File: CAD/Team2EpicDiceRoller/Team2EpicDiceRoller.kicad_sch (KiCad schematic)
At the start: 48 parts, among them J1 Conn_02x03_Odd_Even, J2 Conn_01x16, J3 Conn_01x02_9VBatt, Q1 BS170, Q2 2N2222, SW1 SW_SPDT, SW2 Tilt_Switch, SW3 RotaryEncoder_Switch, SW4 SW_DPST, SW5 SW_LeftMenu, SW6 SW_MidMenu, SW7 SW_Reset, SW8 SW_RightMenu, U1 74HC14, U2 ATmega328P-P, Y1 Crystal_16MHz

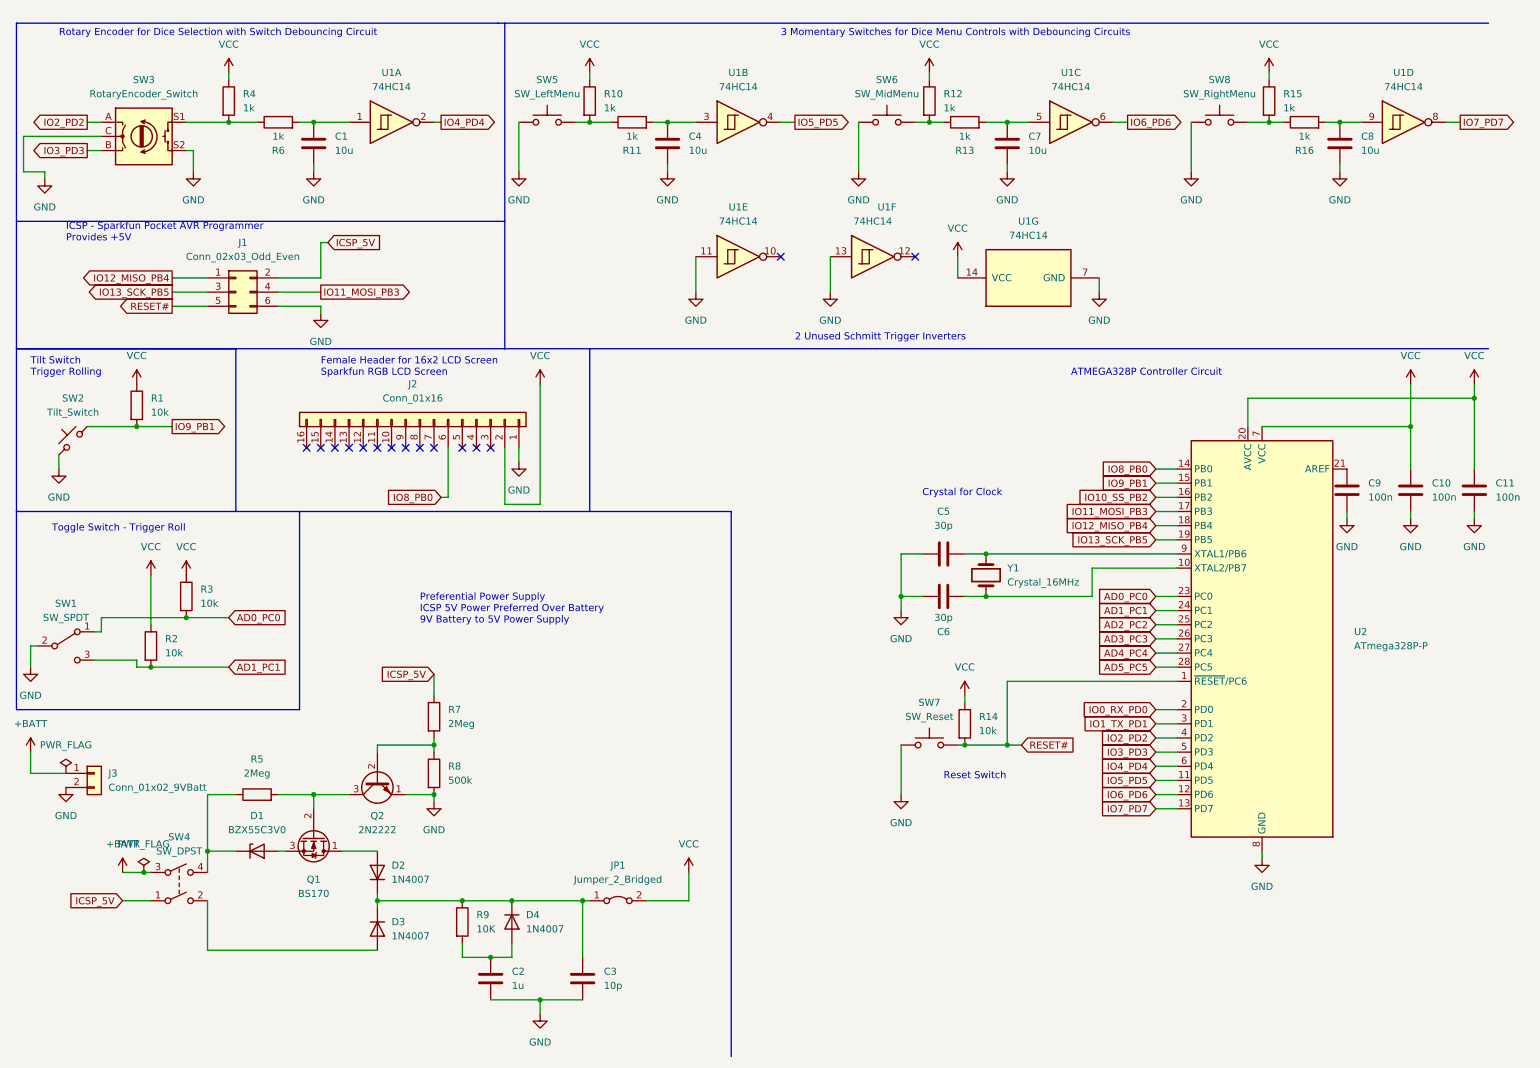
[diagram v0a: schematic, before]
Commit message: Added power supply circuit, barrel jack, logic level shifter
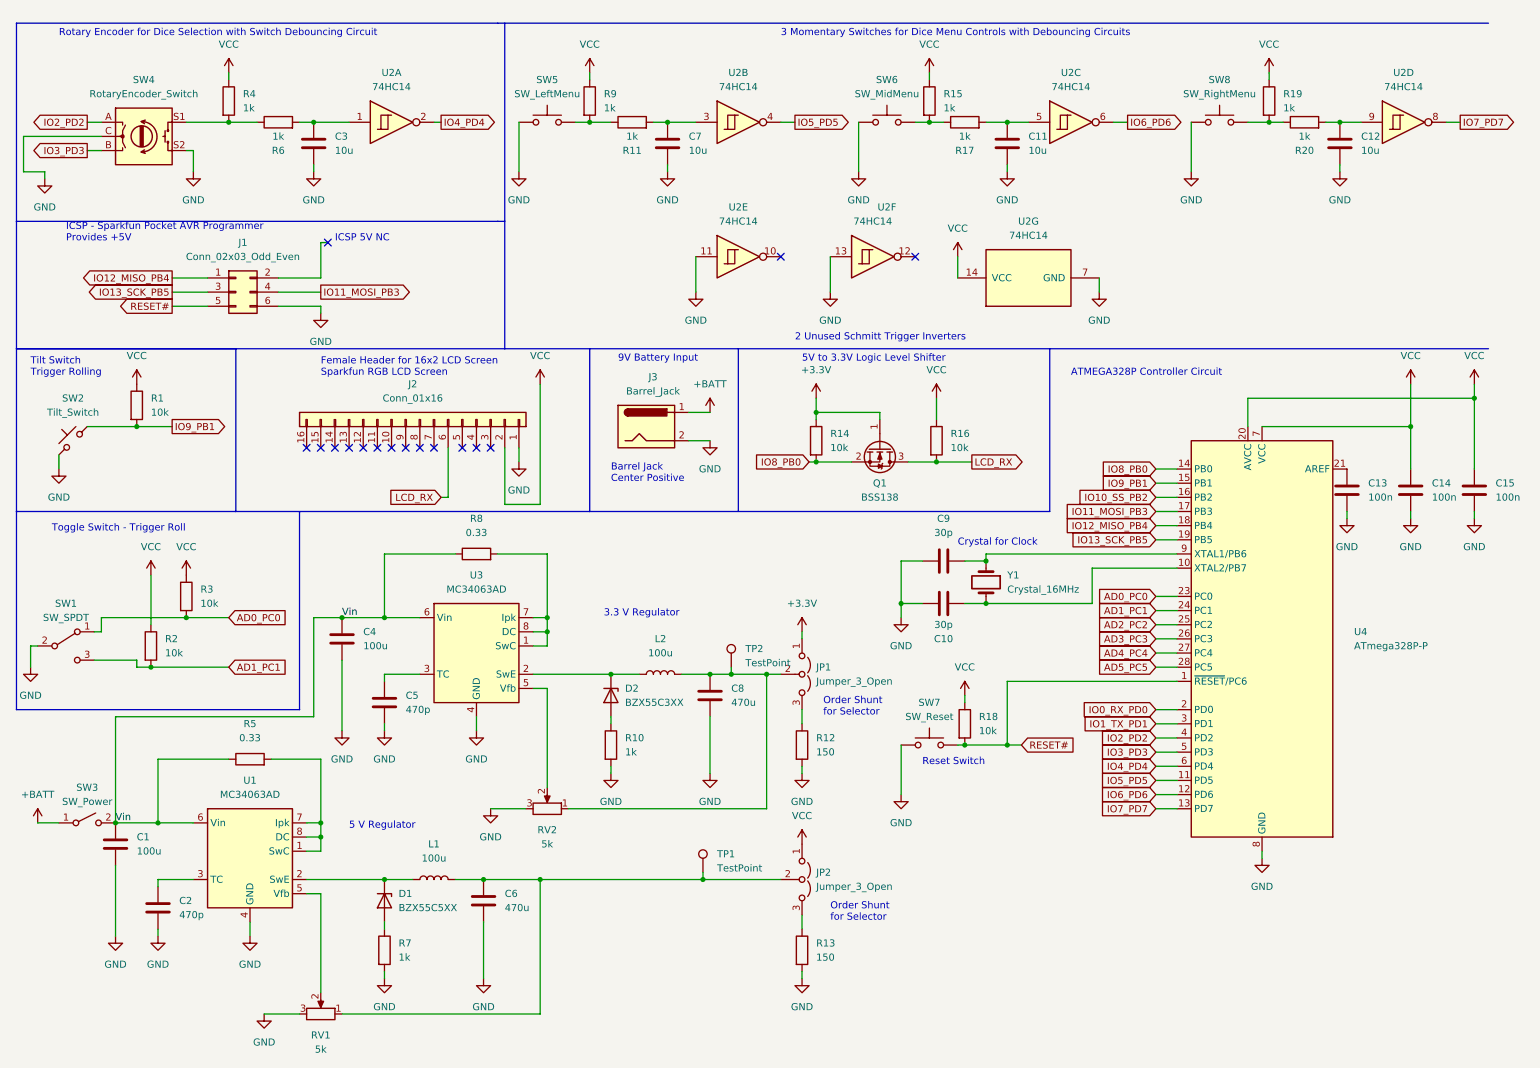
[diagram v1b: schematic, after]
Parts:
- removed D2, D3, D4: 1N4007, Diode_THT:D_DO-41_SOD81_P10.16mm_Horizontal, symbol Diode:1N4007
- removed J3: Conn_01x02_9VBatt, Connector_PinHeader_2.54mm:PinHeader_1x02_P2.54mm_Vertical, symbol Connector_Generic:Conn_01x02
- removed JP1: Jumper_2_Bridged, TestPoint:TestPoint_Bridge_Pitch2.54mm_Drill1.0mm, symbol Jumper:Jumper_2_Bridged
- removed Q1: BS170, Package_TO_SOT_THT:TO-92_Inline, symbol Transistor_FET:BS170
- removed Q2: 2N2222, Package_TO_SOT_THT:TO-92_Inline, symbol Transistor_BJT:PN2222A
- removed R5: 2Meg, Resistor_SMD:R_1206_3216Metric_Pad1.30x1.75mm_HandSolder, symbol Device:R
- removed SW4: SW_DPST, symbol Switch:SW_DPST
- added C4: 100u, Capacitor_SMD:C_1206_3216Metric_Pad1.33x1.80mm_HandSolder, symbol Device:C
- added C5: 470p, Capacitor_SMD:C_1206_3216Metric_Pad1.33x1.80mm_HandSolder, symbol Device:C
- added C6, C8: 470u, Capacitor_SMD:C_1206_3216Metric_Pad1.33x1.80mm_HandSolder, symbol Device:C
- added D2: BZX55C3XX, Diode_THT:D_DO-35_SOD27_P7.62mm_Horizontal, symbol Device:D_Zener
- added J3: Barrel_Jack, symbol Connector:Barrel_Jack
- added JP1, JP2: Jumper_3_Open, symbol Jumper:Jumper_3_Open
- added L1, L2: 100u, symbol Device:L
- added Q1: BSS138, Package_TO_SOT_SMD:SOT-23, symbol Transistor_FET:BSS138
- added R10: 1k, Resistor_SMD:R_1206_3216Metric_Pad1.30x1.75mm_HandSolder, symbol Device:R
- added R12: 150, Resistor_SMD:R_1206_3216Metric_Pad1.30x1.75mm_HandSolder, symbol Device:R
- added R14, R16: 10k, symbol Device:R
- added R8: 0.33, Resistor_SMD:R_1206_3216Metric_Pad1.30x1.75mm_HandSolder, symbol Device:R
- added RV1, RV2: 5k, symbol Device:R_Potentiometer
- added SW3: SW_Power, symbol Switch:SW_SPST
- added TP1, TP2: TestPoint, symbol Connector:TestPoint
- added U1, U3: MC34063AD, Package_SO:SOIC-8_3.9x4.9mm_P1.27mm, symbol Regulator_Switching:MC34063AD
- C1: renamed from C2; value 1u -> 100u
- C2: renamed from C3; value 10p -> 470p
- D1: value BZX55C3V0 -> BZX55C5XX
- R13: renamed from R9; value 10K -> 150
- R5: renamed from R8; value 500k -> 0.33
- R7: value 2Meg -> 1k
- renumbered C6 to C10, C7 to C11, C8 to C12, C9 to C13, C10 to C14, C11 to C15, C1 to C3, C4 to C7, C5 to C9, R12 to R15, R13 to R17, R14 to R18, R15 to R19, R16 to R20, R10 to R9, SW3 to SW4, U1 to U2, U2 to U4
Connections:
- net +BATT: now also J3.1, SW3.1 (A)
- net GND: now also R13.2, R7.2, C4.2, C5.2, C6.2, C8.2, J3.2, R10.2, R12.2, RV1.3, RV2.3, U1.4 (GND), U3.4 (GND); no longer R5.2
- net IO8_PB0: now also Q1.2 (S), R14.2; no longer J2.6 (Pin_6)
- net VCC: now also JP2.1 (A), R16.1
- net at D1.2 (A): now also R7.1
- net Vin: now reaches C1.1
- net Vin: now also R5.1, C4.1, R8.1, SW3.2 (B), U1.6 (Vin), U3.6 (Vin); no longer R13.2
- net at C2.1: now also U1.3 (TC); no longer R13.1
- net at D1.1 (K): now also L1.1, U1.2 (SwE)
- net ICSP_5V: no longer names the net of J1.2 (Pin_2)
- net ICSP_5V: no longer R7.1
- new net: C6.1, JP2.2 (C), L1.2, RV1.1, TP1.1
- new net: JP2.3 (B), R13.1
- new net: R8.2, U3.1 (SwC), U3.7 (Ipk), U3.8 (DC)
- new net: D2.1 (K), L2.1, U3.2 (SwE)
- new net: C5.1, U3.3 (TC)
- new net: RV2.2, U3.5 (Vfb)
- new net: R5.2, U1.1 (SwC), U1.7 (Ipk), U1.8 (DC)
- new net: RV1.2, U1.5 (Vfb)
- new net: JP1.3 (B), R12.1
- new net: C8.1, JP1.2 (C), L2.2, RV2.1, TP2.1
- new net: D2.2 (A), R10.1
- new net +3V3: JP1.1 (A), Q1.1 (G), R14.1
- new net LCD_RX: J2.6 (Pin_6), Q1.3 (D), R16.2
- no-connect marks 15 -> 16
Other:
- note added: "3.3 V Regulator"
- note added: "5 V Regulator"
- note added: "5V to 3.3V Logic Level Shifter"
- note added: "9V Battery Input"
- note added: "Barrel Jack Center Positive"
- note added: "ICSP 5V NC"
- note added: "Order Shunt for Selector"
- note removed: "Preferential Power Supply ICSP 5V Power Preferred Over Battery 9V Battery to 5V Power Supply"
- title: Team 2 - Dice Roller Initial Schematic -> Team 2 - Dice Roller Schematic
- moved on the sheet: C1, C10, C2, C9, D1, R13, R5, R7, Y1

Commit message: Updated schematic
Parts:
- J3: footprint (none) -> Library:BarrelJack_CUI_PJ-037A_Horizontal
- JP1, JP2: footprint (none) -> Connector_PinHeader_2.54mm:PinHeader_1x03_P2.54mm_Vertical
- Q1: footprint Package_TO_SOT_SMD:SOT-23 -> Package_TO_SOT_SMD:SOT-323_SC-70_Handsoldering
- R14, R16: footprint (none) -> Resistor_SMD:R_1206_3216Metric_Pad1.30x1.75mm_HandSolder
- RV1, RV2: footprint (none) -> Library:TRIM_TC33X-2-502E
- SW1: value SW_SPDT -> SW_Toggle_SPDT; footprint (none) -> Library:GoldSun_MTS103_Mini_Toggle_Switch
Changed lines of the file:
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@@
       (effects (font (size 1.27 1.27)) (justify left))
     )
-    (property "Footprint" "" (id 2) (at 155.702 87.63 90)
+    (property "Footprint" "Resistor_SMD:R_1206_3216Metric_Pad1.30x1.75mm_HandSolder" (id 2) (at 155.702 87.63 90)
       (effects (font (size 1.27 1.27)) hide)
     )
@@
       (effects (font (size 1.27 1.27)) (justify left))
     )
-    (property "Footprint" "" (id 2) (at 177.292 87.63 90)
+    (property "Footprint" "Resistor_SMD:R_1206_3216Metric_Pad1.30x1.75mm_HandSolder" (id 2) (at 177.292 87.63 90)
       (effects (font (size 1.27 1.27)) hide)
     )
@@
     (property "Reference" "RV1" (id 0) (at 68.58 194.31 90))
     (property "Value" "5k" (id 1) (at 68.58 196.85 90))
-    (property "Footprint" "" (id 2) (at 68.58 190.5 0)
+    (property "Footprint" "Library:TRIM_TC33X-2-502E" (id 2) (at 68.58 190.5 0)
       (effects (font (size 1.27 1.27)) hide)
     )
@@
     (property "Reference" "RV2" (id 0) (at 109.22 157.48 90))
     (property "Value" "5k" (id 1) (at 109.22 160.02 90))
-    (property "Footprint" "" (id 2) (at 109.22 153.67 0)
+    (property "Footprint" "Library:TRIM_TC33X-2-502E" (id 2) (at 109.22 153.67 0)
       (effects (font (size 1.27 1.27)) hide)
     )
@@
     (in_bom yes) (on_board yes) (fields_autoplaced)
     (property "Reference" "SW1" (id 0) (at 22.86 116.84 0))
-    (property "Value" "SW_SPDT" (id 1) (at 22.86 119.38 0))
-    (property "Footprint" "" (id 2) (at 22.86 124.46 0)
+    (property "Value" "SW_Toggle_SPDT" (id 1) (at 22.86 119.38 0))
+    (property "Footprint" "Library:GoldSun_MTS103_Mini_Toggle_Switch" (id 2) (at 22.86 124.46 0)
       (effects (font (size 1.27 1.27)) hide)
     )
@@
       (effects (font (size 1.27 1.27)) (justify left))
     )
-    (property "Footprint" "" (id 2) (at 154.94 129.54 0)
+    (property "Footprint" "Connector_PinHeader_2.54mm:PinHeader_1x03_P2.54mm_Vertical" (id 2) (at 154.94 129.54 0)
       (effects (font (size 1.27 1.27)) hide)
     )
@@
       (effects (font (size 1.27 1.27)) (justify left))
     )
-    (property "Footprint" "" (id 2) (at 154.94 166.37 0)
+    (property "Footprint" "Connector_PinHeader_2.54mm:PinHeader_1x03_P2.54mm_Vertical" (id 2) (at 154.94 166.37 0)
       (effects (font (size 1.27 1.27)) hide)
     )
@@
     (property "Reference" "Q1" (id 0) (at 168.91 95.25 90))
     (property "Value" "BSS138" (id 1) (at 168.91 97.79 90))
-    (property "Footprint" "Package_TO_SOT_SMD:SOT-23" (id 2) (at 167.005 93.98 0)
+    (property "Footprint" "Package_TO_SOT_SMD:SOT-323_SC-70_Handsoldering" (id 2) (at 167.005 93.98 0)
       (effects (font (size 1.27 1.27) italic) (justify left) hide)
     )
@@
     (property "Reference" "J3" (id 0) (at 128.2065 76.2 0))
     (property "Value" "Barrel_Jack" (id 1) (at 128.2065 78.74 0))
-    (property "Footprint" "" (id 2) (at 128.27 86.106 0)
+    (property "Footprint" "Library:BarrelJack_CUI_PJ-037A_Horizontal" (id 2) (at 128.27 86.106 0)
       (effects (font (size 1.27 1.27)) hide)
     )
@@
     )
     (path "/a22f0e59-c995-4a77-b01f-895393d42f53"
-      (reference "J3") (unit 1) (value "Barrel_Jack") (footprint "")
+      (reference "J3") (unit 1) (value "Barrel_Jack") (footprint "Library:BarrelJack_CUI_PJ-037A_Horizontal")
     )
     (path "/f2ed617e-7a79-41d5-a780-4e2949ba9cf7"
-      (reference "JP1") (unit 1) (value "Jumper_3_Open") (footprint "")
+      (reference "JP1") (unit 1) (value "Jumper_3_Open") (footprint "Connector_PinHeader_2.54mm:PinHeader_1x03_P2.54mm_Vertical")
     )
     (path "/247e2d19-36ad-4a30-8472-65ffcbbb520f"
-      (reference "JP2") (unit 1) (value "Jumper_3_Open") (footprint "")
+      (reference "JP2") (unit 1) (value "Jumper_3_Open") (footprint "Connector_PinHeader_2.54mm:PinHeader_1x03_P2.54mm_Vertical")
     )
     (path "/efd78667-ad9c-4abe-95be-41cfe7b3f9a2"
@@
     )
     (path "/08460420-b30b-45a0-968d-ea36b360168a"
-      (reference "Q1") (unit 1) (value "BSS138") (footprint "Package_TO_SOT_SMD:SOT-23")
+      (reference "Q1") (unit 1) (value "BSS138") (footprint "Package_TO_SOT_SMD:SOT-323_SC-70_Handsoldering")
     )
     (path "/e747d653-0eaf-433e-a919-597f7e917a16"
@@
     )
     (path "/a2c9735e-4a2d-405c-869d-3d050fdc7cf6"
-      (reference "R14") (unit 1) (value "10k") (footprint "")
+      (reference "R14") (unit 1) (value "10k") (footprint "Resistor_SMD:R_1206_3216Metric_Pad1.30x1.75mm_HandSolder")
     )
     (path "/b50c7506-28c1-4c3f-923a-75c412ae6bbe"
@@
     )
     (path "/9c3cb9cb-0b23-44fa-8fdb-b9358cbf94e8"
-      (reference "R16") (unit 1) (value "10k") (footprint "")
+      (reference "R16") (unit 1) (value "10k") (footprint "Resistor_SMD:R_1206_3216Metric_Pad1.30x1.75mm_HandSolder")
     )
     (path "/8e5e8a11-f6ba-43f3-8d91-5e7a896ea9fc"
@@
     )
     (path "/daa876e5-5262-45eb-8eaa-bc6937395761"
-      (reference "RV1") (unit 1) (value "5k") (footprint "")
+      (reference "RV1") (unit 1) (value "5k") (footprint "Library:TRIM_TC33X-2-502E")
     )
     (path "/b0910a92-fb93-4c51-a965-1ce77fd5959f"
-      (reference "RV2") (unit 1) (value "5k") (footprint "")
+      (reference "RV2") (unit 1) (value "5k") (footprint "Library:TRIM_TC33X-2-502E")
     )
     (path "/0202e76d-ed31-4c5e-be5c-d15779b91b8b"
-      (reference "SW1") (unit 1) (value "SW_SPDT") (footprint "")
+      (reference "SW1") (unit 1) (value "SW_Toggle_SPDT") (footprint "Library:GoldSun_MTS103_Mini_Toggle_Switch")
     )
     (path "/a94b1b9e-64b4-4337-907b-28f328893b5b"

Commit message: added footprints for electrolytic capacitor
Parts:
- removed C6, C8: 470u, Capacitor_SMD:C_1206_3216Metric_Pad1.33x1.80mm_HandSolder, symbol Device:C
- added C6, C8: 470u, Capacitor_THT:CP_Radial_D5.0mm_P2.50mm, symbol Device:C_Polarized
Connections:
- net GND: now also C6.2, C8.2
- net at JP2.2 (C), L1.2, RV1.1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: now also C6.1
- net at JP1.2 (C), L2.2, RV2.1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: now also C8.1
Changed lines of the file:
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@@
     (pin "2")
   )
-  (symbol (lib_id "Device:C") (at 97.79 170.18 0) (unit 1)
-    (in_bom yes) (on_board yes)
+  (symbol (lib_id "Device:C_Polarized") (at 97.79 170.18 0) (unit 1)
+    (in_bom yes) (on_board yes) (fields_autoplaced)
     (property "Reference" "C6" (id 0) (at 101.6 168.9099 0)
       (effects (font (size 1.27 1.27)) (justify left))
@@
       (effects (font (size 1.27 1.27)) (justify left))
     )
-    (property "Footprint" "Capacitor_SMD:C_1206_3216Metric_Pad1.33x1.80mm_HandSolder" (id 2) (at 98.7552 173.99 0)
+    (property "Footprint" "Capacitor_THT:CP_Radial_D5.0mm_P2.50mm" (id 2) (at 98.7552 173.99 0)
       (effects (font (size 1.27 1.27)) hide)
     )
@@
     (pin "2")
   )
-  (symbol (lib_id "Device:C") (at 138.43 133.35 0) (unit 1)
-    (in_bom yes) (on_board yes)
+  (symbol (lib_id "Device:C_Polarized") (at 138.43 133.35 0) (unit 1)
+    (in_bom yes) (on_board yes) (fields_autoplaced)
     (property "Reference" "C8" (id 0) (at 142.24 132.0799 0)
       (effects (font (size 1.27 1.27)) (justify left))
@@
       (effects (font (size 1.27 1.27)) (justify left))
     )
-    (property "Footprint" "Capacitor_SMD:C_1206_3216Metric_Pad1.33x1.80mm_HandSolder" (id 2) (at 139.3952 137.16 0)
+    (property "Footprint" "Capacitor_THT:CP_Radial_D5.0mm_P2.50mm" (id 2) (at 139.3952 137.16 0)
       (effects (font (size 1.27 1.27)) hide)
     )
@@
       (reference "C5") (unit 1) (value "470p") (footprint "Capacitor_SMD:C_1206_3216Metric_Pad1.33x1.80mm_HandSolder")
     )
-    (path "/6b887ba2-ce46-4831-904e-c3be4f46b508"
-      (reference "C6") (unit 1) (value "470u") (footprint "Capacitor_SMD:C_1206_3216Metric_Pad1.33x1.80mm_HandSolder")
+    (path "/5742b5fd-3f8d-4d64-bb1a-04db38f14d1d"
+      (reference "C6") (unit 1) (value "470u") (footprint "Capacitor_THT:CP_Radial_D5.0mm_P2.50mm")
     )
     (path "/e430aba8-016f-47fe-86d9-c150d7f518cd"
       (reference "C7") (unit 1) (value "10u") (footprint "Capacitor_SMD:C_1206_3216Metric_Pad1.33x1.80mm_HandSolder")
     )
-    (path "/86f8f59e-fe00-4520-b930-ec0eeb54edf2"
-      (reference "C8") (unit 1) (value "470u") (footprint "Capacitor_SMD:C_1206_3216Metric_Pad1.33x1.80mm_HandSolder")
+    (path "/9c48a684-ed08-4a42-8221-2c4c4eaf77cd"
+      (reference "C8") (unit 1) (value "470u") (footprint "Capacitor_THT:CP_Radial_D5.0mm_P2.50mm")
     )
     (path "/7e5013ac-be8e-44d0-99da-910d44977e25"

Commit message: updated zener diodes and resistor values
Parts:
- D1: value BZX55C5XX -> BZX55C5V1
- D2: value BZX55C3XX -> BZX55C3V9
- R10: value 1k -> 120
- R7: value 1k -> 68
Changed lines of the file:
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@@
       (effects (font (size 1.27 1.27)) (justify left))
     )
-    (property "Value" "1k" (id 1) (at 82.55 180.3399 0)
+    (property "Value" "68" (id 1) (at 82.55 180.3399 0)
       (effects (font (size 1.27 1.27)) (justify left))
     )
@@
       (effects (font (size 1.27 1.27)) (justify left))
     )
-    (property "Value" "1k" (id 1) (at 123.19 143.5099 0)
+    (property "Value" "120" (id 1) (at 123.19 143.5099 0)
       (effects (font (size 1.27 1.27)) (justify left))
     )
@@
       (effects (font (size 1.27 1.27)) (justify left))
     )
-    (property "Value" "BZX55C5XX" (id 1) (at 82.55 171.4499 90)
+    (property "Value" "BZX55C5V1" (id 1) (at 82.55 171.4499 90)
       (effects (font (size 1.27 1.27)) (justify left))
     )
@@
       (effects (font (size 1.27 1.27)) (justify left))
     )
-    (property "Value" "BZX55C3XX" (id 1) (at 123.19 134.6199 90)
+    (property "Value" "BZX55C3V9" (id 1) (at 123.19 134.6199 90)
       (effects (font (size 1.27 1.27)) (justify left))
     )
@@
     )
     (path "/d332a016-8edf-4c9a-8ea4-9d52128a65fe"
-      (reference "D1") (unit 1) (value "BZX55C5XX") (footprint "Diode_THT:D_DO-35_SOD27_P7.62mm_Horizontal")
+      (reference "D1") (unit 1) (value "BZX55C5V1") (footprint "Diode_THT:D_DO-35_SOD27_P7.62mm_Horizontal")
     )
     (path "/c742c256-195d-43d8-87fd-b46ec7a89997"
-      (reference "D2") (unit 1) (value "BZX55C3XX") (footprint "Diode_THT:D_DO-35_SOD27_P7.62mm_Horizontal")
+      (reference "D2") (unit 1) (value "BZX55C3V9") (footprint "Diode_THT:D_DO-35_SOD27_P7.62mm_Horizontal")
     )
     (path "/97500fde-4c78-42dd-ab07-3c6ad623f25a"
@@
     )
     (path "/7f356495-e216-4c39-8078-c83dcfbe350e"
-      (reference "R7") (unit 1) (value "1k") (footprint "Resistor_SMD:R_1206_3216Metric_Pad1.30x1.75mm_HandSolder")
+      (reference "R7") (unit 1) (value "68") (footprint "Resistor_SMD:R_1206_3216Metric_Pad1.30x1.75mm_HandSolder")
     )
     (path "/a36990b2-b2b8-49f9-8a51-8db03ada13fd"
@@
     )
     (path "/7f9781a6-0677-4bee-af04-a4e8cd60f89d"
-      (reference "R10") (unit 1) (value "1k") (footprint "Resistor_SMD:R_1206_3216Metric_Pad1.30x1.75mm_HandSolder")
+      (reference "R10") (unit 1) (value "120") (footprint "Resistor_SMD:R_1206_3216Metric_Pad1.30x1.75mm_HandSolder")
     )
     (path "/128c3cc7-55c7-4ba1-8765-077eb017a110"
